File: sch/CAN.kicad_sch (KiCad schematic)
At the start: 18 parts, among them U2 TJA1051T/3, U3 TJA1051T/3

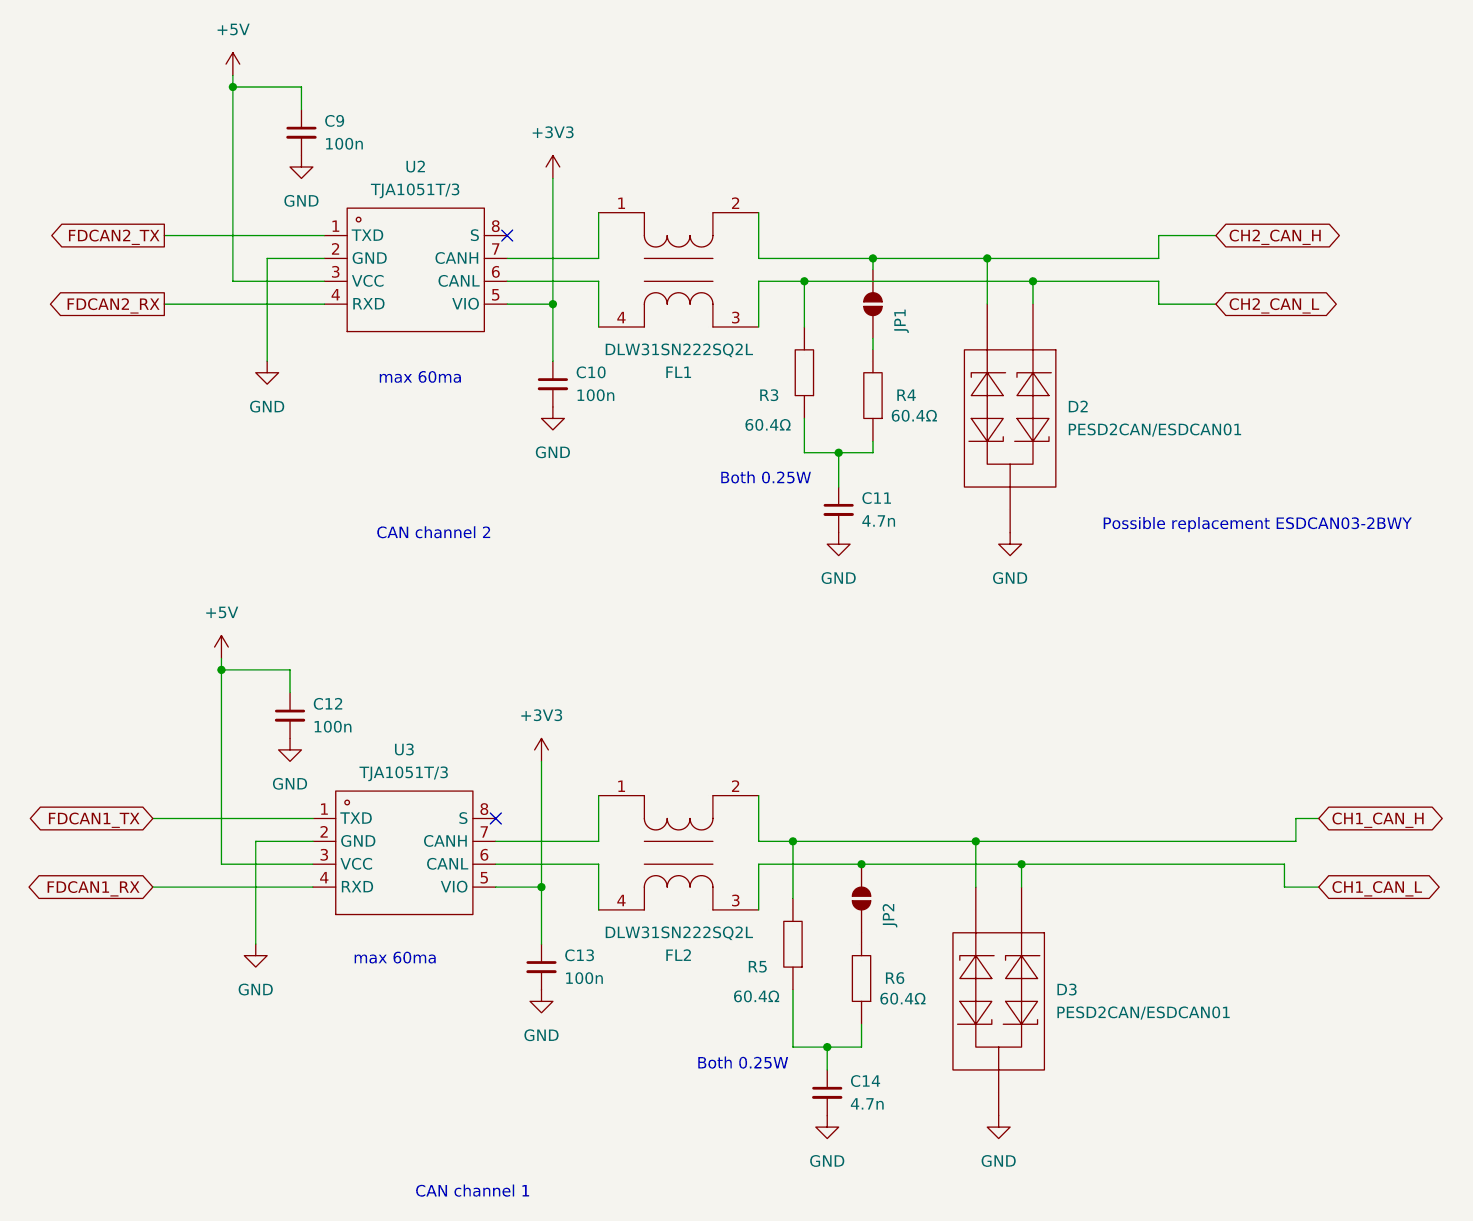
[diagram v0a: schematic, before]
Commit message: v1.1 changes * increase LED resistors as they are too bright * replace solder jumpers with pins * add corresponding 3D models
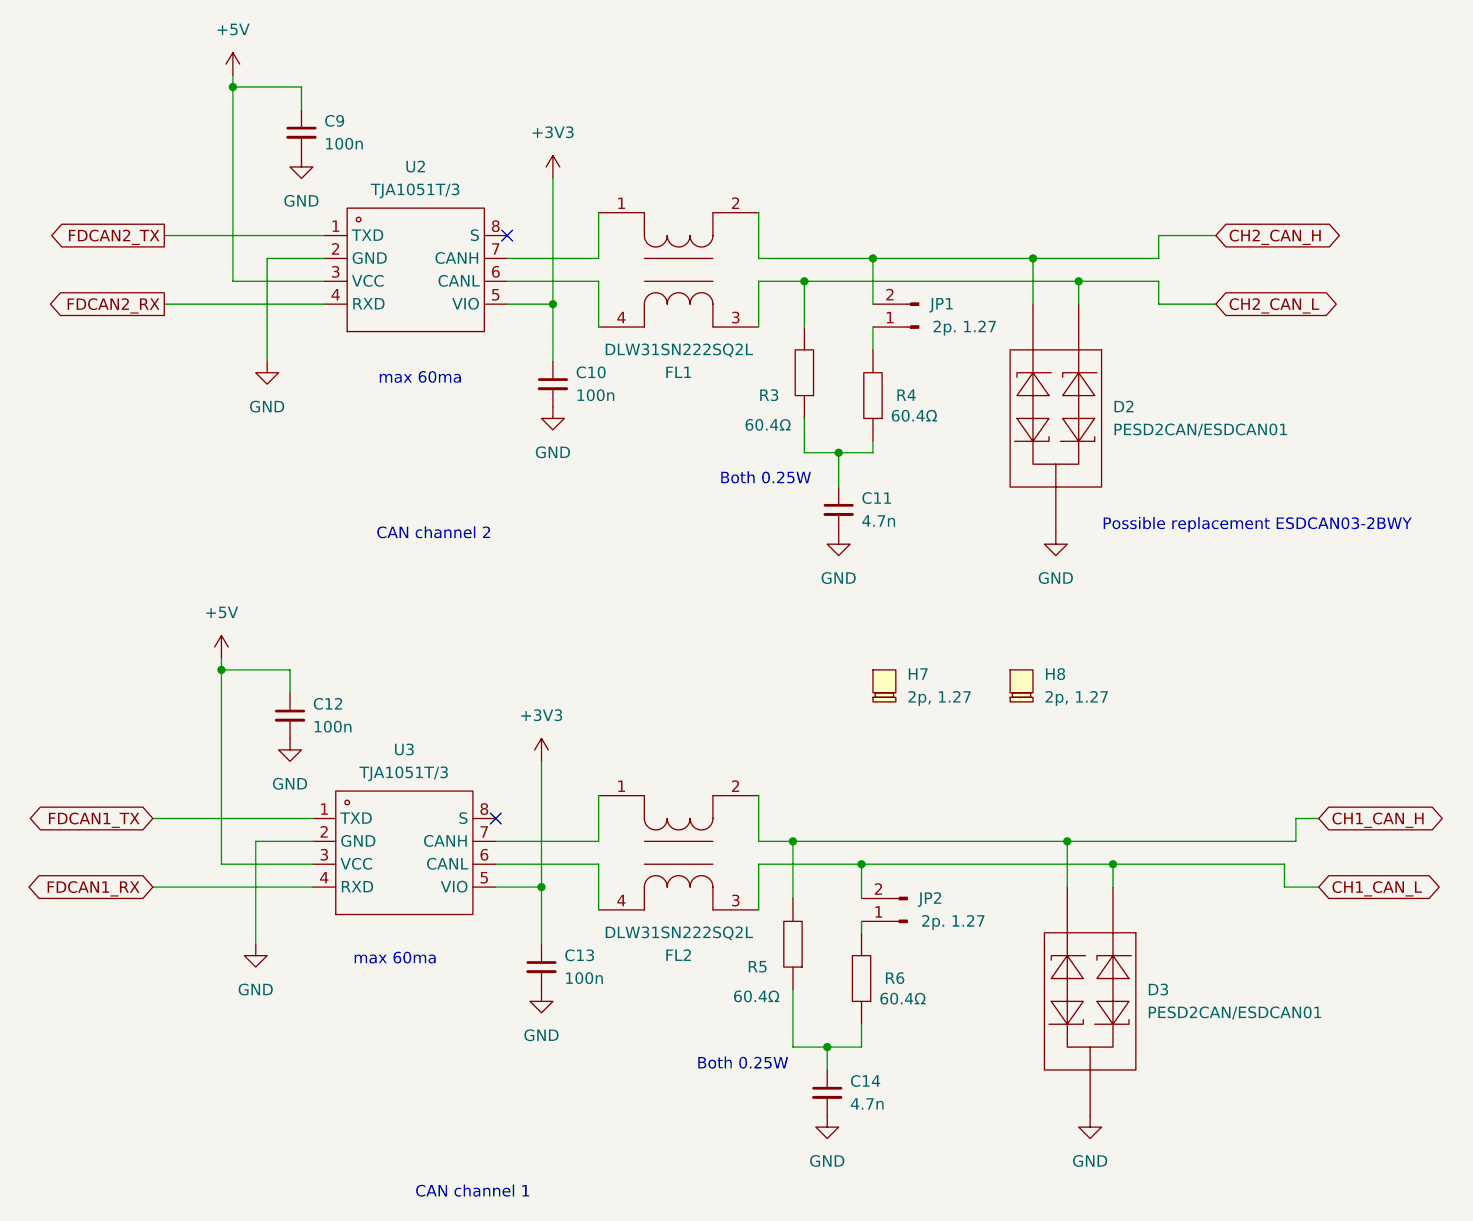
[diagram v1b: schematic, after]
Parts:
- removed JP1, JP2: SolderJumper_2_Open, Jumper:SolderJumper-2_P1.3mm_Open_RoundedPad1.0x1.5mm, symbol Jumper:SolderJumper_2_Open
- added H7, H8: 2p, 1.27, symbol canlogger_custom_lib:Jumper_Shunt
- added JP1, JP2: 2p. 1.27, canlogger_custom_lib:PinHeader_1x02_P1.27mm_Vertical, symbol Connector:Conn_01x02_Pin
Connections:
- net CH1_CAN_L: now also JP2.2 (Pin_2)
- net CH2_CAN_H: now also JP1.2 (Pin_2)
- net at R4.2: now also JP1.1 (Pin_1)
- net at R6.2: now also JP2.1 (Pin_1)
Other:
- title: 2CH CAN  Logger -> Dual Channel CAN Logger
- moved on the sheet: D2, D3
